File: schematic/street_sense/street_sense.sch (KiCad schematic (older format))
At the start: 23 parts, among them J1 USB_B_Micro, Q1 FQP27P06, Q2 PN2222A, Q3 FQP27P06, U1 Lolin_D32_Pro, U2 5V_DC_DC_BOOST, U3 plantower_pms5003, U5 I2C_OLED_128x64, U6 ADS1219, U7 DS3231M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

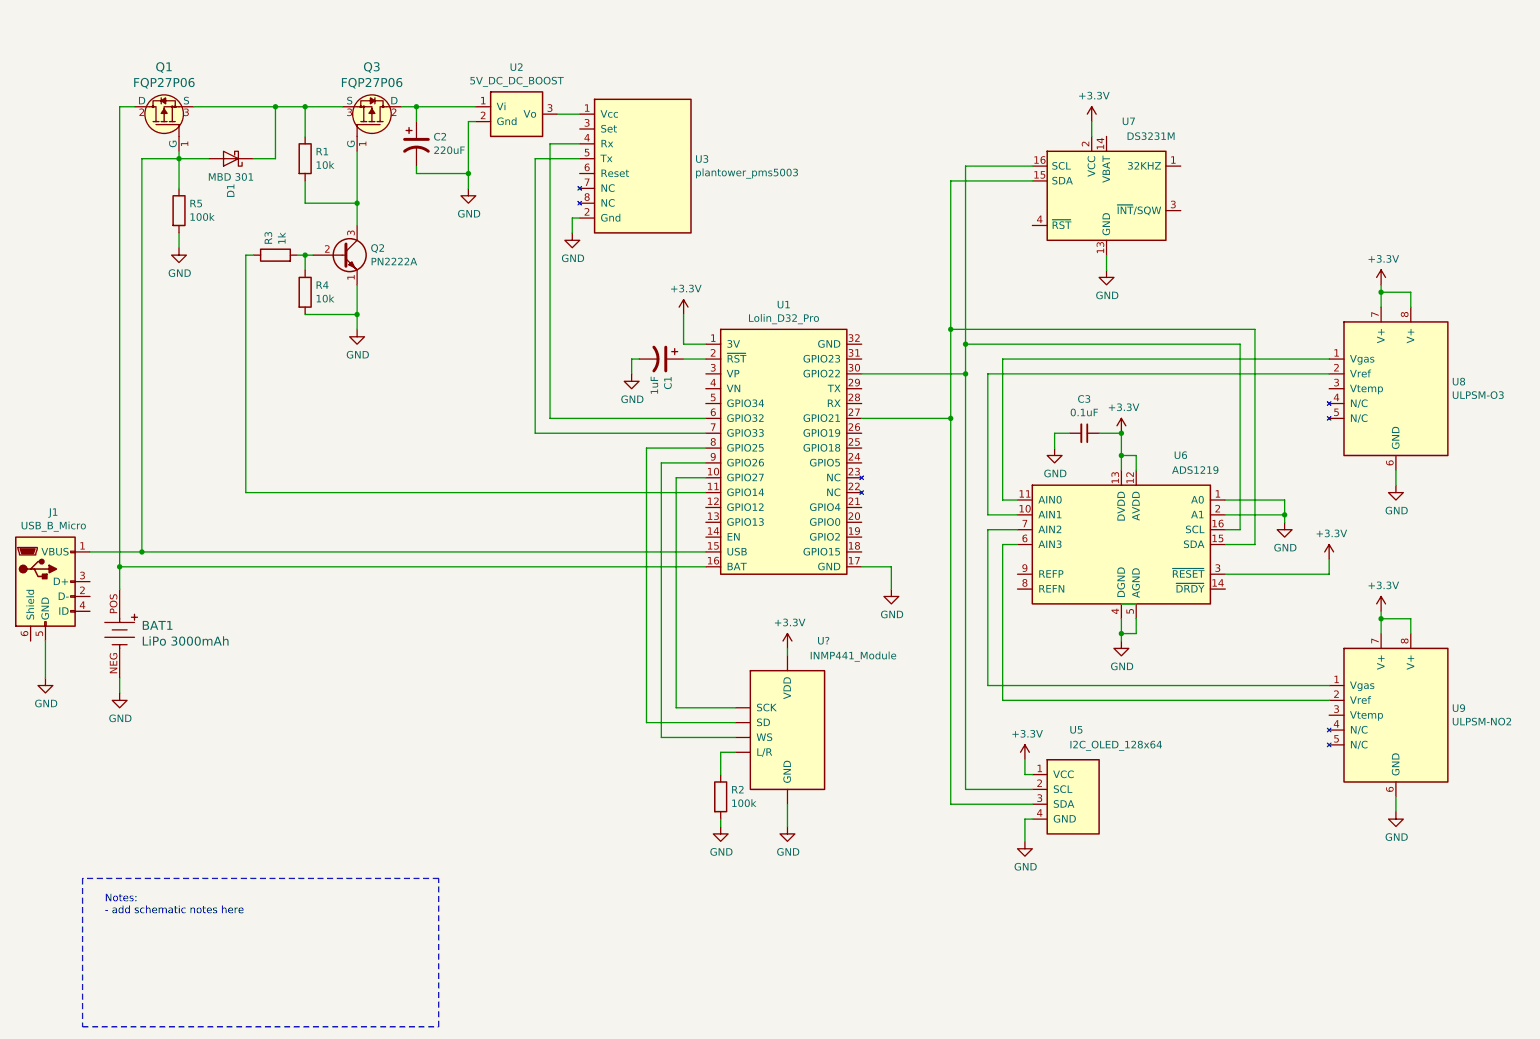
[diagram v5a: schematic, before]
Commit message: added si7021 temperature/humidity sensor
- updated uPy code
- added new symbol to KiCad symbol library
- updated schematic, v07
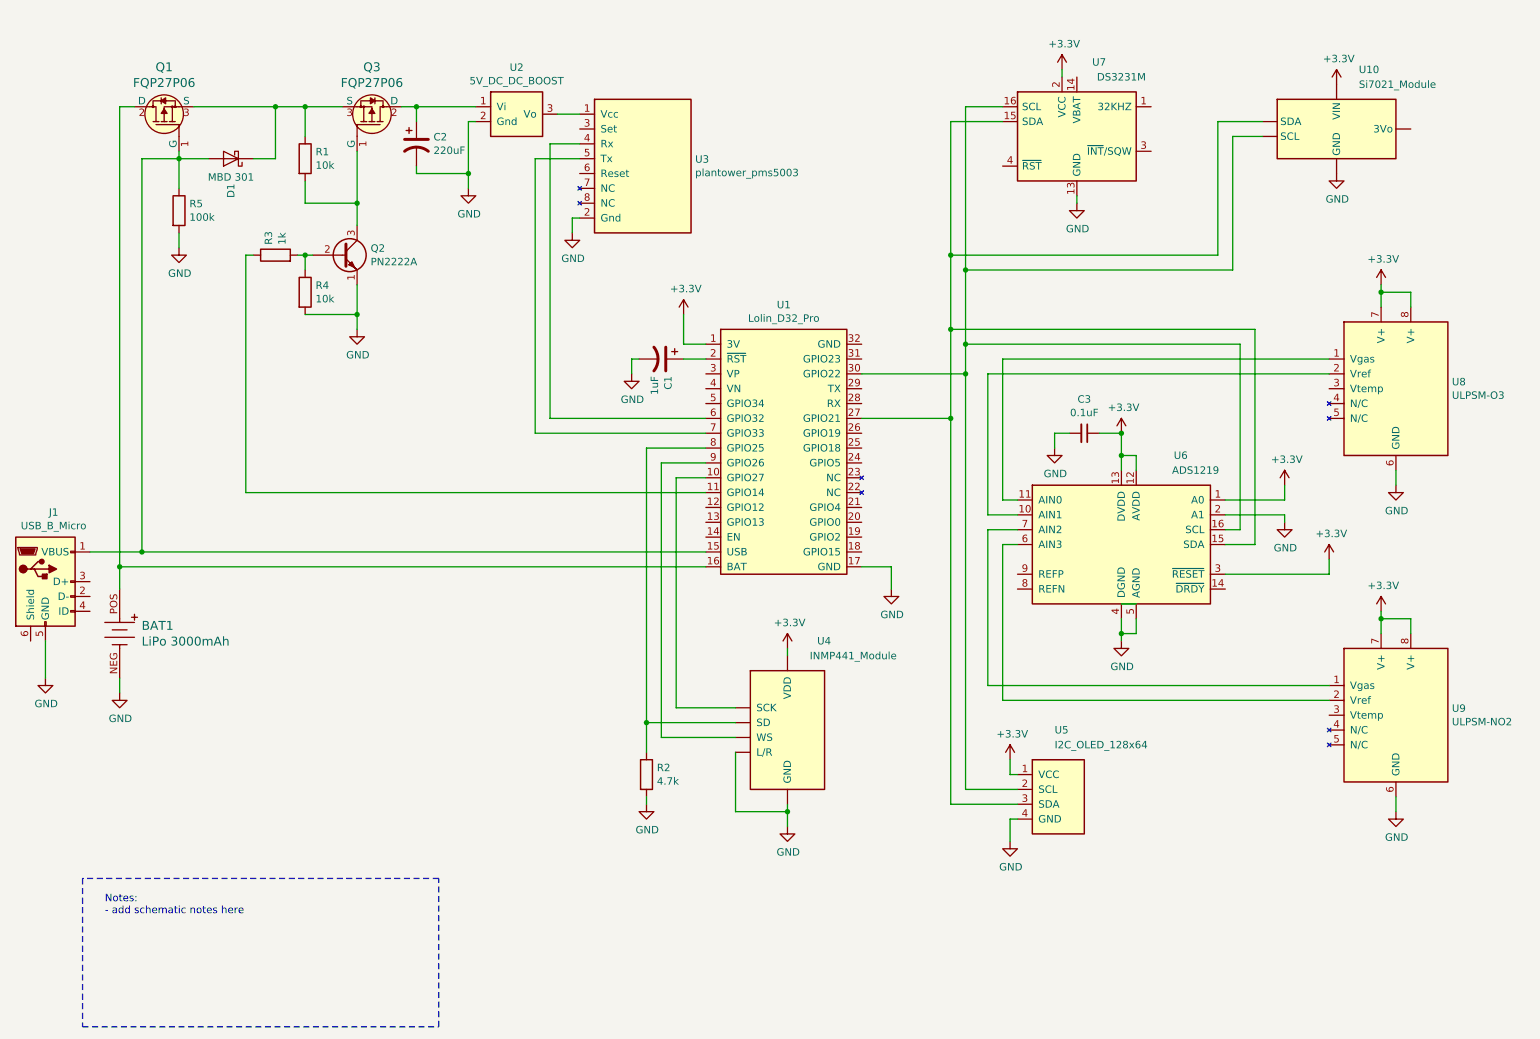
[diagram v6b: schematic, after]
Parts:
- added U10: Si7021_Module, Breakout Module, symbol mike_library:Si7021_Module
- R2: value 100k -> 4.7k
- gave numbers to parts that had none: 1
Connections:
- net +3V3: now also U6.1 (A0), U10.~ (VIN)
- net GND: now also U10.~ (VIN); no longer U6.1 (A0)
- net at U1.27 (GPIO21), U5.3 (SDA), U6.15 (SDA)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: now also U10.~ (VIN)
- net at U1.30 (GPIO22), U5.2 (SCL), U6.16 (SCL)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: now also U10.~ (VIN)
- net at U1.8 (GPIO25), U4.~ (WS): now also R2.1
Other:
- moved on the sheet: R2, U5, U7
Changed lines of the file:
@@
 Sheet 1 1
 Title "Street Sense"
-Date "2019-03-20"
-Rev "v06"
+Date "2019-03-25"
+Rev "v07"
 Comp ""
 Comment1 ""
@@
 $EndComp
 Wire Wire Line
-	6000 6150 6000 6000
+	6000 6150 6000 6050
 Wire Wire Line
 	5450 3600 5050 3600
@@
 L power:GND #PWR07
 U 1 1 5C616822
-P 7600 6250
-F 0 "#PWR07" H 7600 6000 50  0001 C CNN
-F 1 "GND" H 7605 6077 50  0000 C CNN
-F 2 "" H 7600 6250 50  0001 C CNN
-F 3 "" H 7600 6250 50  0001 C CNN
-	1    7600 6250
+P 7500 6250
+F 0 "#PWR07" H 7500 6000 50  0001 C CNN
+F 1 "GND" H 7505 6077 50  0000 C CNN
+F 2 "" H 7500 6250 50  0001 C CNN
+F 3 "" H 7500 6250 50  0001 C CNN
+	1    7500 6250
 	1    0    0    -1
 $EndComp
@@
 L power:+3.3V #PWR06
 U 1 1 5C618F08
-P 7600 5700
-F 0 "#PWR06" H 7600 5550 50  0001 C CNN
-F 1 "+3.3V" H 7615 5873 50  0000 C CNN
-F 2 "" H 7600 5700 50  0001 C CNN
-F 3 "" H 7600 5700 50  0001 C CNN
-	1    7600 5700
-	1    0    0    -1
-$EndComp
-Wire Wire Line
-	7600 5700 7600 5800
+P 7500 5700
+F 0 "#PWR06" H 7500 5550 50  0001 C CNN
+F 1 "+3.3V" H 7515 5873 50  0000 C CNN
+F 2 "" H 7500 5700 50  0001 C CNN
+F 3 "" H 7500 5700 50  0001 C CNN
+	1    7500 5700
+	1    0    0    -1
+$EndComp
+Wire Wire Line
+	7500 5700 7500 5800
 $Comp
 L Timer_RTC:DS3231M U7
 U 1 1 5C619DCE
-P 8150 1900
-F 0 "U7" H 8300 2400 50  0000 C CNN
-F 1 "DS3231M" H 8450 2300 50  0000 C CNN
-F 2 "Package_SO:SOIC-16W_7.5x10.3mm_P1.27mm" H 8150 1300 50  0001 C CNN
-F 3 "http://datasheets.maximintegrated.com/en/ds/DS3231.pdf" H 8420 1950 50  0001 C CNN
-	1    8150 1900
+P 7950 1500
+F 0 "U7" H 8100 2000 50  0000 C CNN
+F 1 "DS3231M" H 8250 1900 50  0000 C CNN
+F 2 "Package_SO:SOIC-16W_7.5x10.3mm_P1.27mm" H 7950 900 50  0001 C CNN
+F 3 "http://datasheets.maximintegrated.com/en/ds/DS3231.pdf" H 8220 1550 50  0001 C CNN
+	1    7950 1500
 	1    0    0    -1
 $EndComp
@@
 	7200 3100 6500 3100
 Wire Wire Line
-	7200 1700 7650 1700
-Wire Wire Line
-	7650 6000 7100 6000
+	7550 6000 7100 6000
 Wire Wire Line
 	7100 3400 6500 3400
-Wire Wire Line
-	7100 1800 7650 1800
 $Comp
 L power:GND #PWR011
 U 1 1 5C631651
-P 8150 2400
-F 0 "#PWR011" H 8150 2150 50  0001 C CNN
-F 1 "GND" H 8155 2227 50  0000 C CNN
-F 2 "" H 8150 2400 50  0001 C CNN
-F 3 "" H 8150 2400 50  0001 C CNN
-	1    8150 2400
-	1    0    0    -1
-$EndComp
-Wire Wire Line
-	8150 2400 8150 2300
+P 7950 1950
+F 0 "#PWR011" H 7950 1700 50  0001 C CNN
+F 1 "GND" H 7955 1777 50  0000 C CNN
+F 2 "" H 7950 1950 50  0001 C CNN
+F 3 "" H 7950 1950 50  0001 C CNN
+	1    7950 1950
+	1    0    0    -1
+$EndComp
+Wire Wire Line
+	7950 1950 7950 1900
 $Comp
 L power:+3.3V #PWR08
 U 1 1 5C6327BC
-P 8050 1400
-F 0 "#PWR08" H 8050 1250 50  0001 C CNN
-F 1 "+3.3V" H 8065 1573 50  0000 C CNN
-F 2 "" H 8050 1400 50  0001 C CNN
-F 3 "" H 8050 1400 50  0001 C CNN
-	1    8050 1400
+P 7850 1050
+F 0 "#PWR08" H 7850 900 50  0001 C CNN
+F 1 "+3.3V" H 7865 1223 50  0000 C CNN
+F 2 "" H 7850 1050 50  0001 C CNN
+F 3 "" H 7850 1050 50  0001 C CNN
+	1    7850 1050
 	1    0    0    -1
 $EndComp
@@
 $EndComp
 Wire Wire Line
-	8050 1400 8050 1500
+	7850 1050 7850 1100
 $Comp
 L power:+3.3V #PWR012
@@
 L Device:R R2
 U 1 1 5C630AD4
-P 5550 5950
-F 0 "R2" H 5620 5996 50  0000 L CNN
-F 1 "100k" H 5620 5905 50  0000 L CNN
-F 2 "" V 5480 5950 50  0001 C CNN
-F 3 "~" H 5550 5950 50  0001 C CNN
-	1    5550 5950
+P 5050 5800
+F 0 "R2" H 5120 5846 50  0000 L CNN
+F 1 "4.7k" H 5120 5755 50  0000 L CNN
+F 2 "" V 4980 5800 50  0001 C CNN
+F 3 "~" H 5050 5800 50  0001 C CNN
+	1    5050 5800
 	1    0    0    -1
 $EndComp
@@
 L power:GND #PWR016
 U 1 1 5C6325CC
-P 5550 6150
-F 0 "#PWR016" H 5550 5900 50  0001 C CNN
-F 1 "GND" H 5555 5977 50  0000 C CNN
-F 2 "" H 5550 6150 50  0001 C CNN
-F 3 "" H 5550 6150 50  0001 C CNN
-	1    5550 6150
-	1    0    0    -1
-$EndComp
-Wire Wire Line
-	5550 5650 5550 5800
-Wire Wire Line
-	5550 6150 5550 6100
+P 5050 6000
+F 0 "#PWR016" H 5050 5750 50  0001 C CNN
+F 1 "GND" H 5055 5827 50  0000 C CNN
+F 2 "" H 5050 6000 50  0001 C CNN
+F 3 "" H 5050 6000 50  0001 C CNN
+	1    5050 6000
+	1    0    0    -1
+$EndComp
+Wire Wire Line
+	5050 6000 5050 5950
 Wire Notes Line
 	1250 6500 1250 7500
@@
 $EndComp
 Wire Wire Line
-	7100 3400 7100 6000
-Wire Wire Line
 	8250 4650 8350 4650
 Wire Wire Line
@@
 $EndComp
 Wire Wire Line
-	8950 3950 9350 3950
-Wire Wire Line
-	9350 3950 9350 4050
-Wire Wire Line
 	8950 4050 9350 4050
-Connection ~ 9350 4050
 Wire Wire Line
 	9350 4050 9350 4100
@@
 Connection ~ 7100 2800
 Wire Wire Line
-	7100 2800 7100 3400
-Wire Wire Line
 	9050 2900 7200 2900
-Wire Wire Line
-	7200 3100 7200 2900
 Connection ~ 7200 2900
 Wire Wire Line
@@
 L mike_library:I2C_OLED_128x64 U5
 U 1 1 5C611EC8
-P 7950 5650
-F 0 "U5" H 7900 5800 50  0000 L CNN
-F 1 "I2C_OLED_128x64" H 7900 5700 50  0000 L CNN
-F 2 "" H 7900 5600 50  0001 C CNN
-F 3 "" H 7900 5600 50  0001 C CNN
-	1    7950 5650
-	1    0    0    -1
-$EndComp
-Wire Wire Line
-	7200 5900 7650 5900
-Wire Wire Line
-	7650 6100 7600 6100
-Wire Wire Line
-	7600 6100 7600 6250
-Wire Wire Line
-	7600 5800 7650 5800
+P 7850 5650
+F 0 "U5" H 7800 5800 50  0000 L CNN
+F 1 "I2C_OLED_128x64" H 7800 5700 50  0000 L CNN
+F 2 "" H 7800 5600 50  0001 C CNN
+F 3 "" H 7800 5600 50  0001 C CNN
+	1    7850 5650
+	1    0    0    -1
+$EndComp
+Wire Wire Line
+	7550 6100 7500 6100
+Wire Wire Line
+	7500 6100 7500 6250
+Wire Wire Line
+	7500 5800 7550 5800
 Wire Wire Line
 	8950 4450 9650 4450
@@
 $EndComp
 Wire Wire Line
-	7200 1700 7200 2900
-Wire Wire Line
-	7100 1800 7100 2800
-Wire Wire Line
 	7200 3100 7200 5900
 Wire Wire Line
@@
 	8250 3650 8250 3750
 $Comp
-L mike_library:INMP441_Module U?
+L mike_library:INMP441_Module U4
 U 1 1 5C92A64F
 P 6000 5000
-F 0 "U?" H 6200 5100 50  0000 L CNN
+F 0 "U4" H 6200 5100 50  0000 L CNN
 F 1 "INMP441_Module" H 6150 5000 50  0000 L CNN
 F 2 "" H 6000 5000 50  0001 C CNN
@@
 $EndComp
 Wire Wire Line
-	5550 5650 5650 5650
-Wire Wire Line
 	5250 5350 5650 5350
 Wire Wire Line
@@
 Wire Wire Line
 	6000 4950 6000 5000
+Wire Wire Line
+	5050 5450 5050 5650
+Connection ~ 5050 5450
+Wire Wire Line
+	5650 5650 5650 6050
+Wire Wire Line
+	5650 6050 6000 6050
+Connection ~ 6000 6050
+Wire Wire Line
+	6000 6050 6000 6000
+$Comp
+L power:+3.3V #PWR019
+U 1 1 5C994EB9
+P 9350 3850
+F 0 "#PWR019" H 9350 3700 50  0001 C CNN
+F 1 "+3.3V" H 9365 4023 50  0000 C CNN
+F 2 "" H 9350 3850 50  0001 C CNN
+F 3 "" H 9350 3850 50  0001 C CNN
+	1    9350 3850
+	1    0    0    -1
+$EndComp
+Wire Wire Line
+	8950 3950 9350 3950
+Wire Wire Line
+	9350 3950 9350 3850
+$Comp
+L mike_library:Si7021_Module U10
+U 1 1 5C99F1F0
+P 9700 1450
+F 0 "U10" H 9850 1850 50  0000 L CNN
+F 1 "Si7021_Module" H 9850 1750 50  0000 L CNN
+F 2 "Breakout Module" H 9700 1050 50  0001 C CNN
+F 3 "https://www.adafruit.com/product/3251" H 9500 1750 50  0001 C CNN
+	1    9700 1450
+	1    0    0    -1
+$EndComp
+Wire Wire Line
+	7100 3400 7100 6000
+Wire Wire Line
+	7550 5900 7200 5900
+Wire Wire Line
+	7200 3100 7200 2900
+Wire Wire Line
+	7100 2800 7100 3400
+$Comp
+L power:+3.3V #PWR020
+U 1 1 5C9CF1AE
+P 9700 1150
+F 0 "#PWR020" H 9700 1000 50  0001 C CNN
+F 1 "+3.3V" H 9715 1323 50  0000 C CNN
+F 2 "" H 9700 1150 50  0001 C CNN
+F 3 "" H 9700 1150 50  0001 C CNN
+	1    9700 1150
+	1    0    0    -1
+$EndComp
+Wire Wire Line
+	7200 1300 7450 1300
+Wire Wire Line
+	7200 1300 7200 2400
+Wire Wire Line
+	7450 1400 7100 1400
+Wire Wire Line
+	7100 1400 7100 2300
+Wire Wire Line
+	7100 2300 8900 2300
+Wire Wire Line
+	8900 2300 8900 1400
+Wire Wire Line
+	8900 1400 9200 1400
+Connection ~ 7100 2300
+Wire Wire Line
+	7100 2300 7100 2800
+Wire Wire Line
+	9200 1500 9000 1500
+Wire Wire Line
+	9000 1500 9000 2400
+Wire Wire Line
+	9000 2400 7200 2400
+Connection ~ 7200 2400
+Wire Wire Line
+	7200 2400 7200 2900
+$Comp
+L power:GND #PWR021
+U 1 1 5C9CF1E9
+P 9700 1750
+F 0 "#PWR021" H 9700 1500 50  0001 C CNN
+F 1 "GND" H 9705 1577 50  0000 C CNN
+F 2 "" H 9700 1750 50  0001 C CNN
+F 3 "" H 9700 1750 50  0001 C CNN
+	1    9700 1750
+	1    0    0    -1
+$EndComp
 $EndSCHEMATC

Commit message: Incremental improvements to measurement performance of O3 and NO2 sensors
Hardware schematic changes:
- separate 3.3V analog supply for O3, NO2, and ADC components
- ~DRDY signal to ESP32 GPIO34

MicroPython changes:
- ~DRDY signal used with interrupt to read ADC values (replaces I2C polling)
- average of 100 samples used to calculate Vref and Vgas measurements
- O3 and NO2 concentrations calculated in parts-per-billion(ppb)
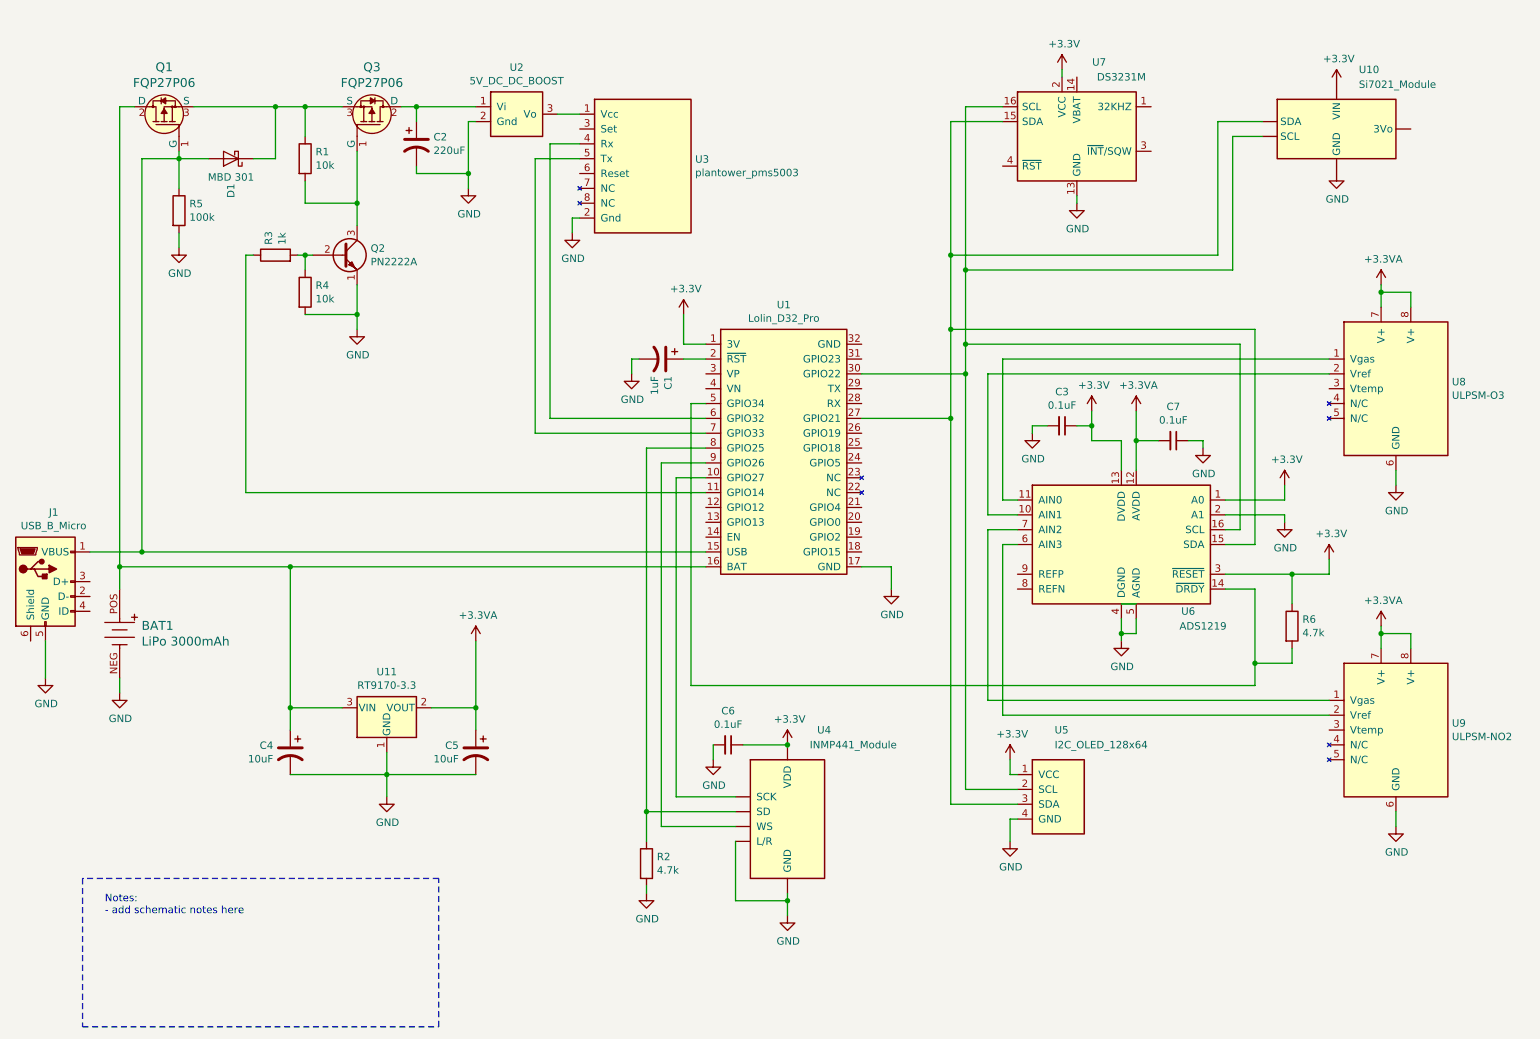
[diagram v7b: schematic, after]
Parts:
- added C4, C5: 10uF, symbol Device:CP1
- added C6, C7: 0.1uF, symbol Device:C_Small
- added R6: 4.7k, symbol Device:R
- added U11: RT9170-3.3, Package_TO_SOT_SMD:TO-252-3_TabPin2, symbol mike_library:RT9170-3.3
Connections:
- net +3V3: now also C6.1, R6.1; no longer U6.12 (AVDD), U8.7 (V+), U8.8 (V+), U9.7 (V+), U9.8 (V+)
- net GND: now also C4.2, C5.2, C6.2, C7.1, U11.1 (GND)
- net at BAT1.POS, Q1.2 (D), U1.16 (BAT): now also C4.1, U11.3 (VIN)
- net at U1.5 (GPIO34): now also U6.14 (~DRDY), R6.2
- new net +3.3VA: C5.1, C7.2, U11.2 (VOUT), U6.12 (AVDD), U8.7 (V+), U8.8 (V+), U9.7 (V+), U9.8 (V+)
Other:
- moved on the sheet: C3, R2, U4, U9
